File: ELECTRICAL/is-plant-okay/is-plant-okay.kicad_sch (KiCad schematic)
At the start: 0 parts

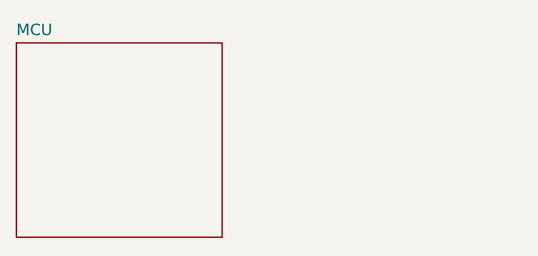
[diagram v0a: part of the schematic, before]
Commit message: feat: minor pin fixes, add camera moduel to schematic
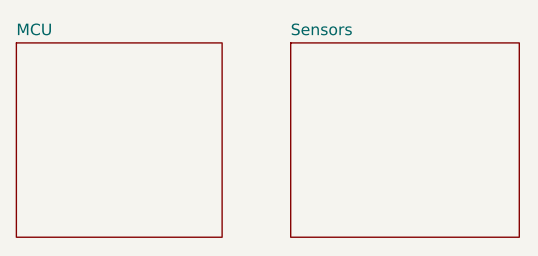
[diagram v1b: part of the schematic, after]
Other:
- added sheet Sensors (sensors.kicad_sch)
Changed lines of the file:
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@@
 	(paper "A4")
+	(sheet
+		(at 137.16 50.8)
+		(size 25.4 21.59)
+		(exclude_from_sim no)
+		(in_bom yes)
+		(on_board yes)
+		(dnp no)
+		(fields_autoplaced yes)
+		(stroke
+			(width 0.1524)
+			(type solid)
+		)
+		(fill
+			(color 0 0 0 0.0000)
+		)
+		(property "Sheetname" "Sensors"
+			(at 137.16 50.0884 0)
+			(effects
+				(font
+					(size 1.27 1.27)
+				)
+				(justify left bottom)
+			)
+		)
+		(property "Sheetfile" "sensors.kicad_sch"
+			(at 137.16 72.9746 0)
+			(effects
+				(font
+					(size 1.27 1.27)
+				)
+				(justify left top)
+				(hide yes)
+			)
+		)
+		(instances
+			(project "is-plant-okay"
+				(path "/ac51c2f9-77a4-4b89-b63f-6e0ba02b1e45"
+					(page "4")
+				)
+			)
+		)
+	)
 	(sheet
 		(at 74.93 50.8)

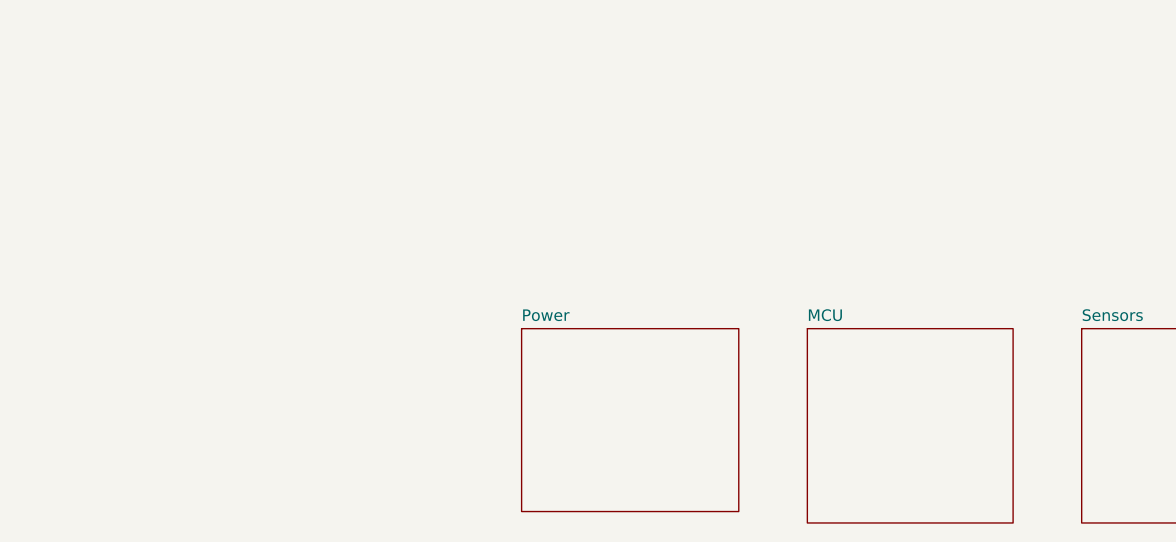
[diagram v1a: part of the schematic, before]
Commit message: feat: add lora, rtc, coin cell, tft screen to schematic
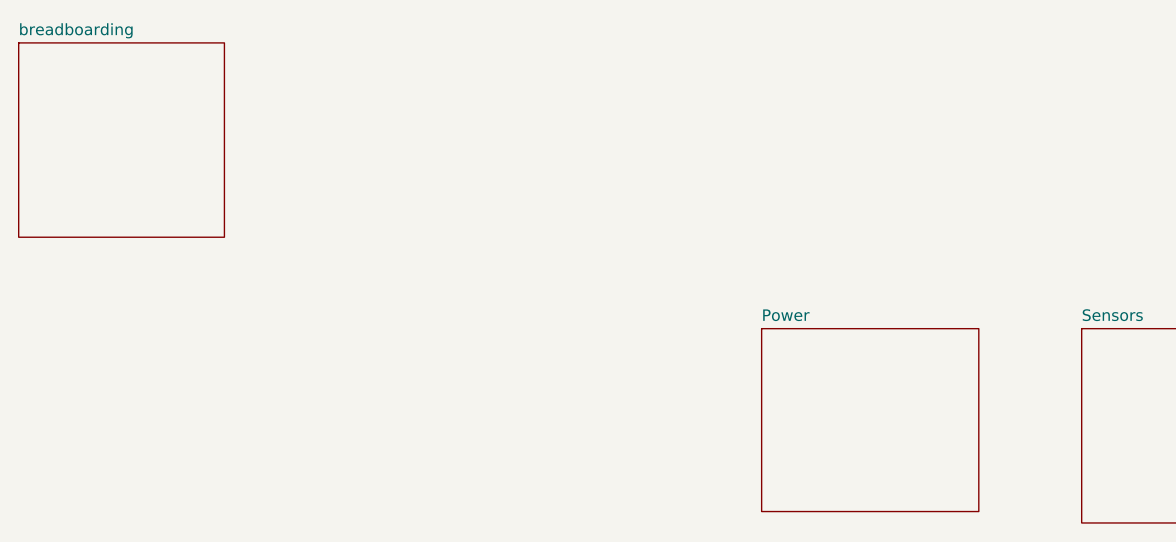
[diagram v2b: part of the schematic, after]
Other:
- sheet MCU renamed breadboarding
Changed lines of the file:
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@@
 	)
 	(sheet
-		(at 74.93 50.8)
+		(at 101.6 50.8)
 		(size 24.13 20.32)
 		(exclude_from_sim no)
@@
 		)
 		(property "Sheetname" "Power"
-			(at 74.93 50.0884 0)
+			(at 101.6 50.0884 0)
 			(effects
 				(font
@@
 		)
 		(property "Sheetfile" "Power.kicad_sch"
-			(at 74.93 71.7046 0)
+			(at 101.6 71.7046 0)
 			(effects
 				(font
@@
 	)
 	(sheet
-		(at 106.68 50.8)
+		(at 19.05 19.05)
 		(size 22.86 21.59)
 		(exclude_from_sim no)
@@
 			(color 0 0 0 0.0000)
 		)
-		(property "Sheetname" "MCU"
-			(at 106.68 50.0884 0)
+		(property "Sheetname" "breadboarding"
+			(at 19.05 18.3384 0)
 			(effects
 				(font
@@
 		)
 		(property "Sheetfile" "mcu.kicad_sch"
-			(at 106.68 72.9746 0)
+			(at 19.05 41.2246 0)
 			(effects
 				(font

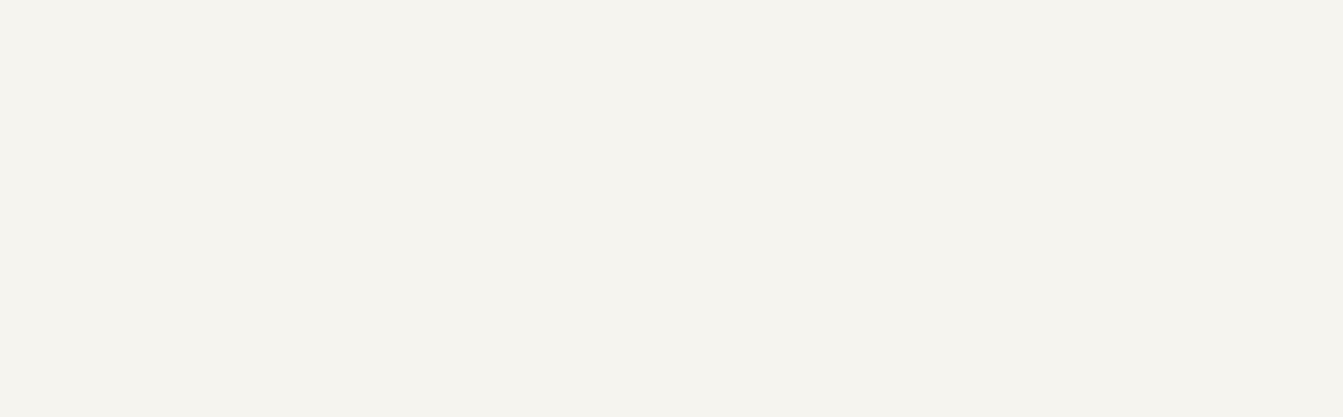
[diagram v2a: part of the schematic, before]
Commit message: feat: add schematic and footprints for ds3234 and ninab306
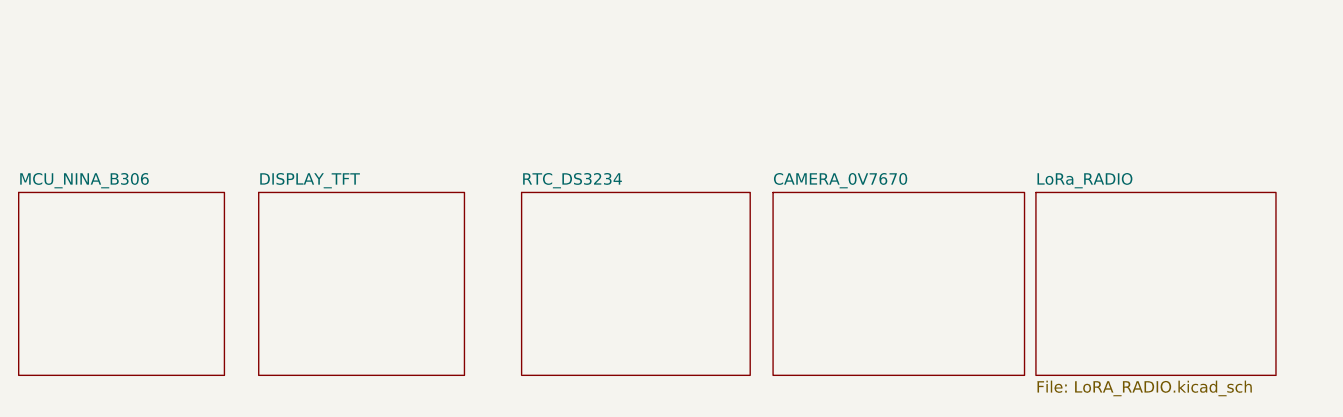
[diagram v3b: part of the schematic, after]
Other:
- added sheet CAMERA_0V7670 (CAMERA_0V7670.kicad_sch)
- added sheet DISPLAY_TFT (DISPLAY_TFT.kicad_sch)
- added sheet LoRa_RADIO (LoRA_RADIO.kicad_sch)
- added sheet MCU_NINA_B306 (MCU_NINA_B306.kicad_sch)
- added sheet RTC_DS3234 (RTC_DS3234.kicad_sch)
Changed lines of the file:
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@@
 	(paper "A4")
+	(sheet
+		(at 130.81 111.76)
+		(size 26.67 20.32)
+		(exclude_from_sim no)
+		(in_bom yes)
+		(on_board yes)
+		(dnp no)
+		(fields_autoplaced yes)
+		(stroke
+			(width 0.1524)
+			(type solid)
+		)
+		(fill
+			(color 0 0 0 0.0000)
+		)
+		(property "Sheetname" "LoRa_RADIO"
+			(at 130.81 111.0484 0)
+			(effects
+				(font
+					(size 1.27 1.27)
+				)
+				(justify left bottom)
+			)
+		)
+		(property "Sheetfile" "LoRA_RADIO.kicad_sch"
+			(at 130.81 132.6646 0)
+			(effects
+				(font
+					(size 1.27 1.27)
+				)
+				(justify left top)
+			)
+		)
+		(instances
+			(project "is-plant-okay"
+				(path "/ac51c2f9-77a4-4b89-b63f-6e0ba02b1e45"
+					(page "9")
+				)
+			)
+		)
+	)
+	(sheet
+		(at 73.66 111.76)
+		(size 25.4 20.32)
+		(exclude_from_sim no)
+		(in_bom yes)
+		(on_board yes)
+		(dnp no)
+		(fields_autoplaced yes)
+		(stroke
+			(width 0.1524)
+			(type solid)
+		)
+		(fill
+			(color 0 0 0 0.0000)
+		)
+		(property "Sheetname" "RTC_DS3234"
+			(at 73.66 111.0484 0)
+			(effects
+				(font
+					(size 1.27 1.27)
+				)
+				(justify left bottom)
+			)
+		)
+		(property "Sheetfile" "RTC_DS3234.kicad_sch"
+			(at 73.66 132.6646 0)
+			(effects
+				(font
+					(size 1.27 1.27)
+				)
+				(justify left top)
+				(hide yes)
+			)
+		)
+		(instances
+			(project "is-plant-okay"
+				(path "/ac51c2f9-77a4-4b89-b63f-6e0ba02b1e45"
+					(page "7")
+				)
+			)
+		)
+	)
+	(sheet
+		(at 44.45 111.76)
+		(size 22.86 20.32)
+		(exclude_from_sim no)
+		(in_bom yes)
+		(on_board yes)
+		(dnp no)
+		(fields_autoplaced yes)
+		(stroke
+			(width 0.1524)
+			(type solid)
+		)
+		(fill
+			(color 0 0 0 0.0000)
+		)
+		(property "Sheetname" "DISPLAY_TFT"
+			(at 44.45 111.0484 0)
+			(effects
+				(font
+					(size 1.27 1.27)
+				)
+				(justify left bottom)
+			)
+		)
+		(property "Sheetfile" "DISPLAY_TFT.kicad_sch"
+			(at 44.45 132.6646 0)
+			(effects
+				(font
+					(size 1.27 1.27)
+				)
+				(justify left top)
+				(hide yes)
+			)
+		)
+		(instances
+			(project "is-plant-okay"
+				(path "/ac51c2f9-77a4-4b89-b63f-6e0ba02b1e45"
+					(page "6")
+				)
+			)
+		)
+	)
 	(sheet
 		(at 137.16 50.8)
@@
 	)
 	(sheet
+		(at 101.6 111.76)
+		(size 27.94 20.32)
+		(exclude_from_sim no)
+		(in_bom yes)
+		(on_board yes)
+		(dnp no)
+		(fields_autoplaced yes)
+		(stroke
+			(width 0.1524)
+			(type solid)
+		)
+		(fill
+			(color 0 0 0 0.0000)
+		)
+		(property "Sheetname" "CAMERA_0V7670"
+			(at 101.6 111.0484 0)
+			(effects
+				(font
+					(size 1.27 1.27)
+				)
+				(justify left bottom)
+			)
+		)
+		(property "Sheetfile" "CAMERA_0V7670.kicad_sch"
+			(at 101.6 132.6646 0)
+			(effects
+				(font
+					(size 1.27 1.27)
+				)
+				(justify left top)
+				(hide yes)
+			)
+		)
+		(instances
+			(project "is-plant-okay"
+				(path "/ac51c2f9-77a4-4b89-b63f-6e0ba02b1e45"
+					(page "8")
+				)
+			)
+		)
+	)
+	(sheet
 		(at 101.6 50.8)
 		(size 24.13 20.32)
@@
 				)
 			)
+		)
+	)
+	(sheet
+		(at 17.78 111.76)
+		(size 22.86 20.32)
+		(exclude_from_sim no)
+		(in_bom yes)
+		(on_board yes)
+		(dnp no)
+		(fields_autoplaced yes)
+		(stroke
+			(width 0.1524)
+			(type solid)
+		)
+		(fill
+			(color 0 0 0 0.0000)
+		)
+		(property "Sheetname" "MCU_NINA_B306"
+			(at 17.78 111.0484 0)
+			(effects
+				(font
+					(size 1.27 1.27)
+				)
+				(justify left bottom)
+			)
+		)
+		(property "Sheetfile" "MCU_NINA_B306.kicad_sch"
+			(at 17.78 132.6646 0)
+			(effects
+				(font
+					(size 1.27 1.27)
+				)
+				(justify left top)
+				(hide yes)
+			)
+		)
+		(instances
+			(project "is-plant-okay"
+				(path "/ac51c2f9-77a4-4b89-b63f-6e0ba02b1e45"
+					(page "5")
+				)
+			)

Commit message: feat: add lora
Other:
- added sheet USB_C_3.3V (USB_C_3-3V.kicad_sch)
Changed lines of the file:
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@@
+	)
+	(sheet
+		(at 161.29 111.76)
+		(size 29.21 20.32)
+		(exclude_from_sim no)
+		(in_bom yes)
+		(on_board yes)
+		(dnp no)
+		(fields_autoplaced yes)
+		(stroke
+			(width 0.1524)
+			(type solid)
+		)
+		(fill
+			(color 0 0 0 0.0000)
+		)
+		(property "Sheetname" "USB_C_3.3V"
+			(at 161.29 111.0484 0)
+			(effects
+				(font
+					(size 1.27 1.27)
+				)
+				(justify left bottom)
+			)
+		)
+		(property "Sheetfile" "USB_C_3-3V.kicad_sch"
+			(at 161.29 132.6646 0)
+			(effects
+				(font
+					(size 1.27 1.27)
+				)
+				(justify left top)
+				(hide yes)
+			)
+		)
+		(instances
+			(project "is-plant-okay"
+				(path "/ac51c2f9-77a4-4b89-b63f-6e0ba02b1e45"
+					(page "10")
+				)
+			)
+		)
 	)
 	(sheet

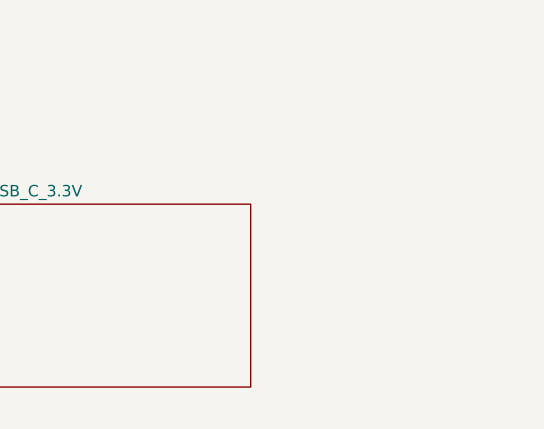
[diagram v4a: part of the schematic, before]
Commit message: feat: add ldo and power management IC
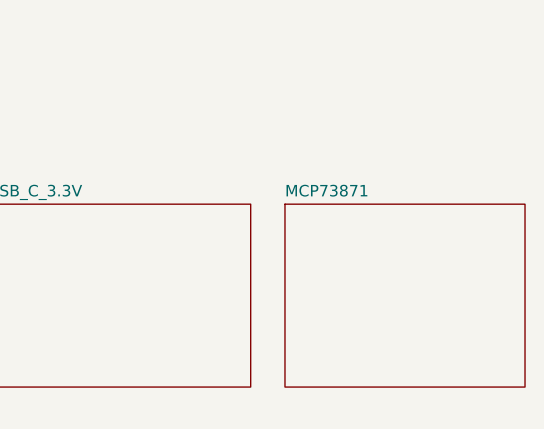
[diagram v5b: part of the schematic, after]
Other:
- added sheet MCP73871 (MCP73871.kicad_sch)
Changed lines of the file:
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@@
+	)
+	(sheet
+		(at 194.31 111.76)
+		(size 26.67 20.32)
+		(exclude_from_sim no)
+		(in_bom yes)
+		(on_board yes)
+		(dnp no)
+		(fields_autoplaced yes)
+		(stroke
+			(width 0.1524)
+			(type solid)
+		)
+		(fill
+			(color 0 0 0 0.0000)
+		)
+		(property "Sheetname" "MCP73871"
+			(at 194.31 111.0484 0)
+			(effects
+				(font
+					(size 1.27 1.27)
+				)
+				(justify left bottom)
+			)
+		)
+		(property "Sheetfile" "MCP73871.kicad_sch"
+			(at 194.31 132.6646 0)
+			(effects
+				(font
+					(size 1.27 1.27)
+				)
+				(justify left top)
+				(hide yes)
+			)
+		)
+		(instances
+			(project "is-plant-okay"
+				(path "/ac51c2f9-77a4-4b89-b63f-6e0ba02b1e45"
+					(page "11")
+				)
+			)
+		)
 	)
 	(sheet

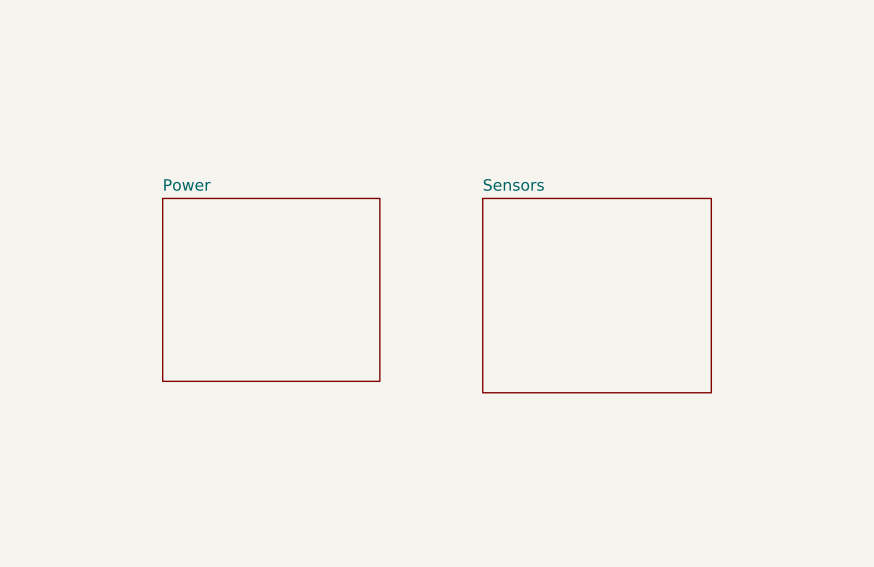
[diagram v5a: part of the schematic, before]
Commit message: feat: add ldo and power management IC
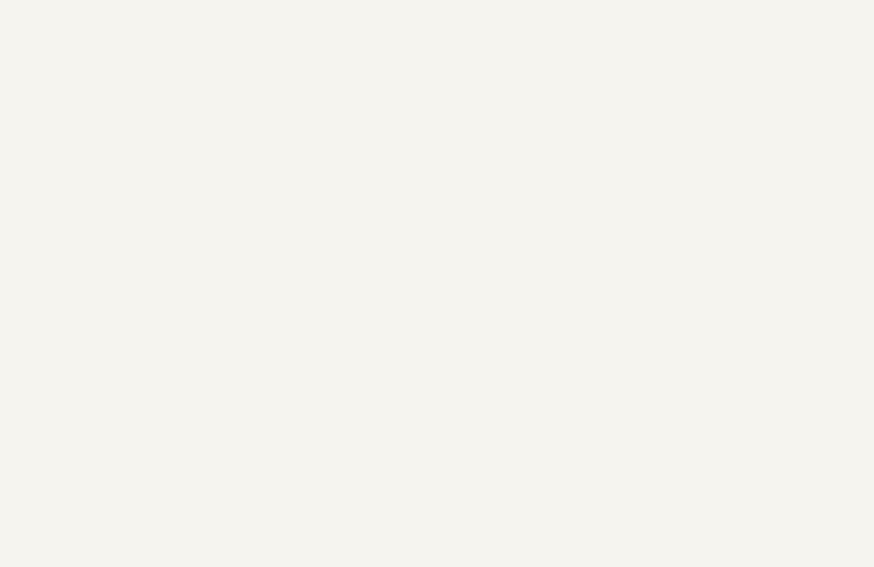
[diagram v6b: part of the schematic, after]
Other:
- removed sheet Power
- removed sheet Sensors
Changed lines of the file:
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@@
-	)
-	(sheet
-		(at 137.16 50.8)
-		(size 25.4 21.59)
-		(exclude_from_sim no)
-		(in_bom yes)
-		(on_board yes)
-		(dnp no)
-		(fields_autoplaced yes)
-		(stroke
-			(width 0.1524)
-			(type solid)
-		)
-		(fill
-			(color 0 0 0 0.0000)
-		)
-		(property "Sheetname" "Sensors"
-			(at 137.16 50.0884 0)
-			(effects
-				(font
-					(size 1.27 1.27)
-				)
-				(justify left bottom)
-			)
-		)
-		(property "Sheetfile" "sensors.kicad_sch"
-			(at 137.16 72.9746 0)
-			(effects
-				(font
-					(size 1.27 1.27)
-				)
-				(justify left top)
-				(hide yes)
-			)
-		)
-		(instances
-			(project "is-plant-okay"
-				(path "/ac51c2f9-77a4-4b89-b63f-6e0ba02b1e45"
-					(page "4")
-				)
-			)
-		)
 	)
 	(sheet
@@
 				)
 			)
-		)
-	)
-	(sheet
-		(at 101.6 50.8)
-		(size 24.13 20.32)
-		(exclude_from_sim no)
-		(in_bom yes)
-		(on_board yes)
-		(dnp no)
-		(fields_autoplaced yes)
-		(stroke
-			(width 0.1524)
-			(type solid)
-		)
-		(fill
-			(color 0 0 0 0.0000)
-		)
-		(property "Sheetname" "Power"
-			(at 101.6 50.0884 0)
-			(effects
-				(font
-					(size 1.27 1.27)
-				)
-				(justify left bottom)
-			)
-		)
-		(property "Sheetfile" "Power.kicad_sch"
-			(at 101.6 71.7046 0)
-			(effects
-				(font
-					(size 1.27 1.27)
-				)
-				(justify left top)
-				(hide yes)
-			)
-		)
-		(instances
-			(project "is-plant-okay"
-				(path "/ac51c2f9-77a4-4b89-b63f-6e0ba02b1e45"
-					(page "2")
-				)
-			)

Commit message: feat: finished schematics
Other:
- removed sheet breadboarding
- sheet CAMERA_0V7670 ports: added 3.3V, CAM_D0, CAM_D1, CAM_D2, CAM_D3, CAM_D4, CAM_D5, CAM_D6, CAM_D7, CAM_PWDN, CAM_RST, HREF, PCLK, SIOC, SIOD, VSYNC, XCLK; removed none
- sheet DISPLAY_TFT ports: added 3.3V, TFT_BACKLIGHT, TFT_CS, TFT_DC, TFT_MISO, TFT_MOSI, TFT_SCLK, TFT_SDCS; removed none
- sheet LoRa_RADIO ports: added 3.3V, LORA_BUSY, LORA_CS, LORA_DIO1, LORA_MISO, LORA_MOSI, LORA_RF_SW, LORA_SCLK; removed none
- sheet MCP73871 ports: added 3.3V, 5V; removed none
- sheet MCU_NINA_B306 ports: added 3.3V, 5V, CAM_D0, CAM_D1, CAM_D2, CAM_D3, CAM_D4, CAM_D5, CAM_D6, CAM_D7, CAM_PWDN, CAM_RST, DATA_NEG, DATA_POS, HREF, LORA_BUSY, LORA_CS, LORA_DIO1, LORA_MISO, LORA_MOSI, LORA_RF_SW, LORA_SCLK, PCLK, RTC_CS, RTC_MISO, RTC_MOSI, RTC_SCLK, SIOC, SIOD, TFT_BACKLIGHT, TFT_CS, TFT_DC, TFT_MISO, TFT_MOSI, TFT_SCLK, TFT_SDCS, VSYNC, XCLK; removed none
- sheet RTC_DS3234 ports: added 3.3V, RTC_CS, RTC_MISO, RTC_MOSI, RTC_SCLK; removed none
- sheet USB_C_3.3V ports: added 5V, DATA_NEG, DATA_POS; removed none
